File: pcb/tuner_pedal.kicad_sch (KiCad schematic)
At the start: 35 parts, among them J1 SWD, J2 Fermion 1.8" TFT LCD, J3 UART, J4 Potentiometer, SW1 SW_Push, SW2 SW_Push, U1 STM32F411CEUx, Y1 25MHz 9pF

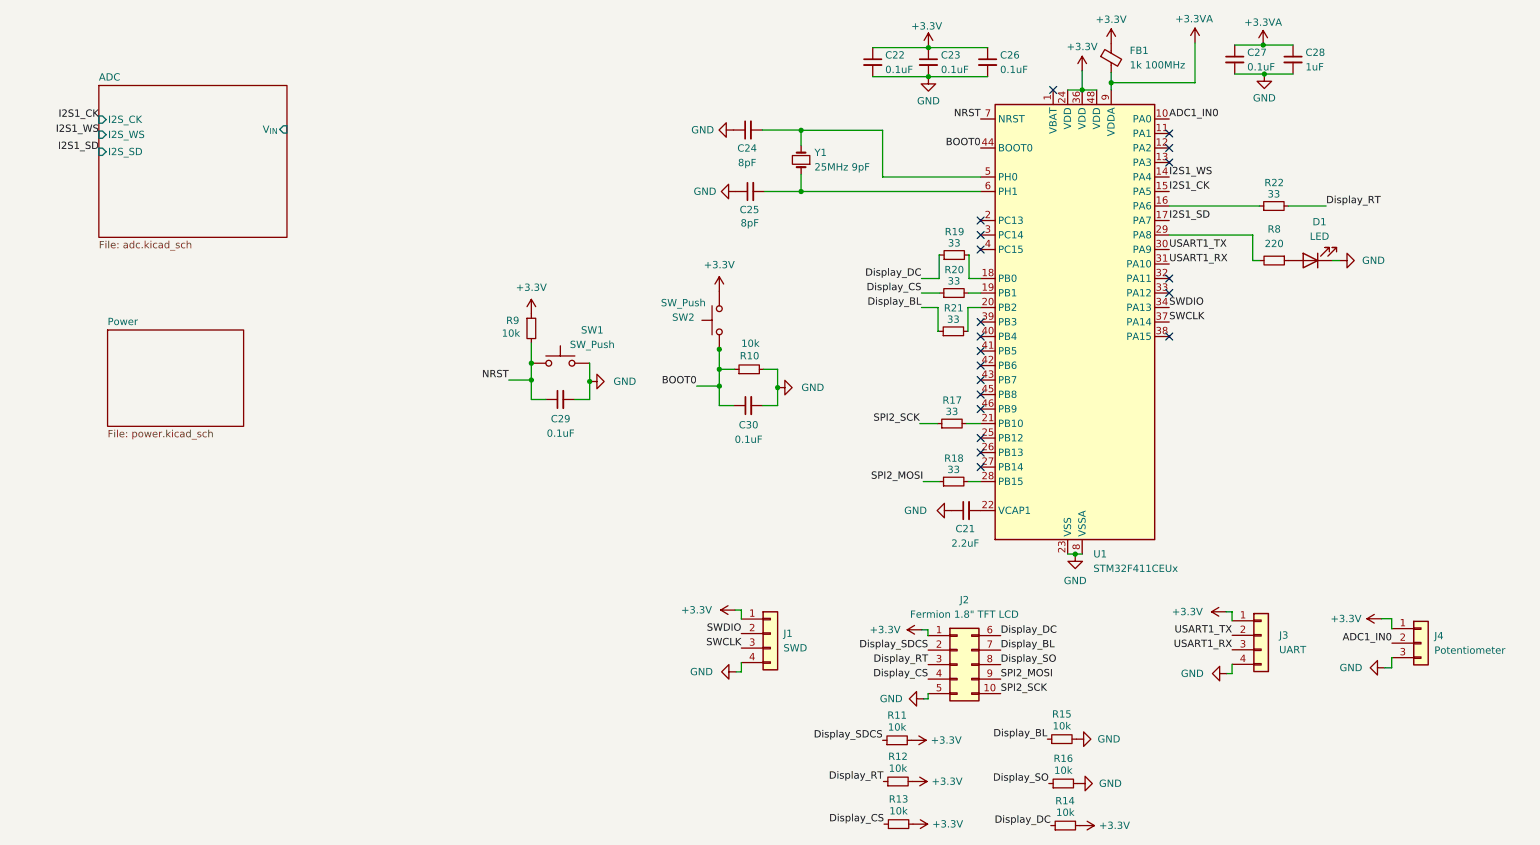
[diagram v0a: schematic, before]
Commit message: Made MCU sheet
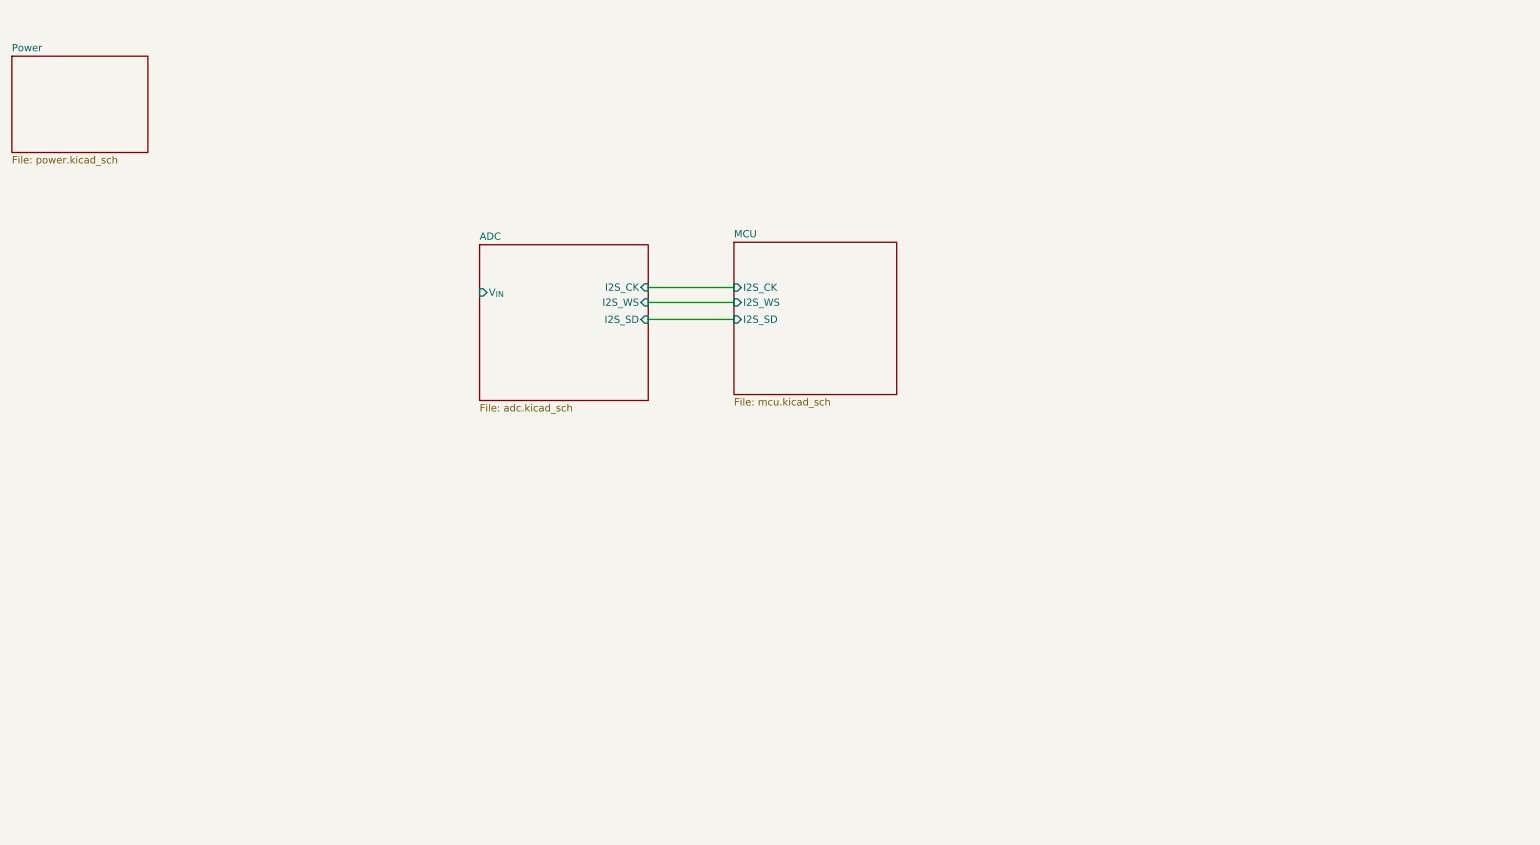
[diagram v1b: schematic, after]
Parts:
- removed C21: 2.2uF, symbol Device:C_Small
- removed C22, C23, C26, C27, C29, C30: 0.1uF, symbol Device:C_Small
- removed C24, C25: 8pF, symbol Device:C_Small
- removed C28: 1uF, symbol Device:C_Small
- removed D1: LED, symbol Device:LED
- removed FB1: 1k 100MHz, symbol Device:FerriteBead_Small
- removed J1: SWD, Connector_PinHeader_2.54mm:PinHeader_1x04_P2.54mm_Vertical, symbol Connector_Generic:Conn_01x04
- removed J2: Fermion 1.8" TFT LCD, Connector_PinHeader_2.54mm:PinHeader_2x05_P2.54mm_Vertical, symbol Connector_Generic:Conn_02x05_Top_Bottom
- removed J3: UART, Connector_PinHeader_2.54mm:PinHeader_1x04_P2.54mm_Vertical, symbol Connector_Generic:Conn_01x04
- removed J4: Potentiometer, Connector_PinSocket_2.54mm:PinSocket_1x03_P2.54mm_Vertical, symbol Connector_Generic:Conn_01x03
- removed R10, R11, R12, R13, R14, R15, R16, R9: 10k, symbol Device:R_Small
- removed R17, R18, R19, R20, R21, R22: 33, symbol Device:R_Small
- removed R8: 220, symbol Device:R_Small
- removed SW1, SW2: SW_Push, Button_Switch_SMD:SW_SPST_Omron_B3FS-100xP, symbol Switch:SW_Push
- removed U1: STM32F411CEUx, Package_DFN_QFN:QFN-48-1EP_7x7mm_P0.5mm_EP5.6x5.6mm, symbol MCU_ST_STM32F4:STM32F411CEUx
- removed Y1: 25MHz 9pF, symbol Device:Crystal_Small
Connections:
- no-connect marks 20 -> 0
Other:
- added sheet MCU (mcu.kicad_sch)

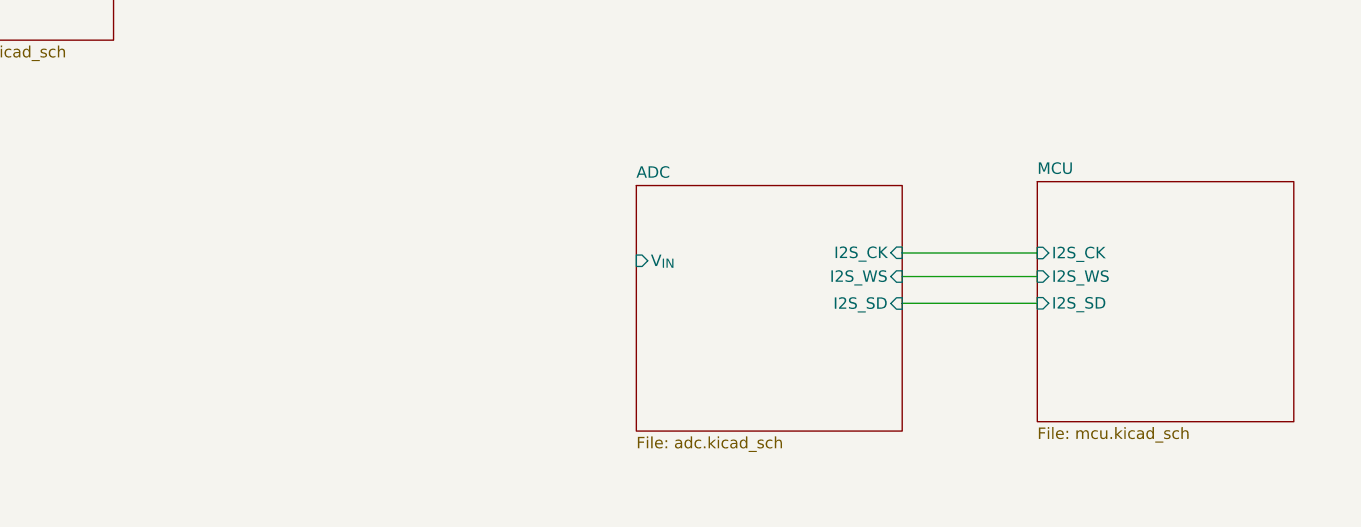
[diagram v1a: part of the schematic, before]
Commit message: Brought in analog frontend
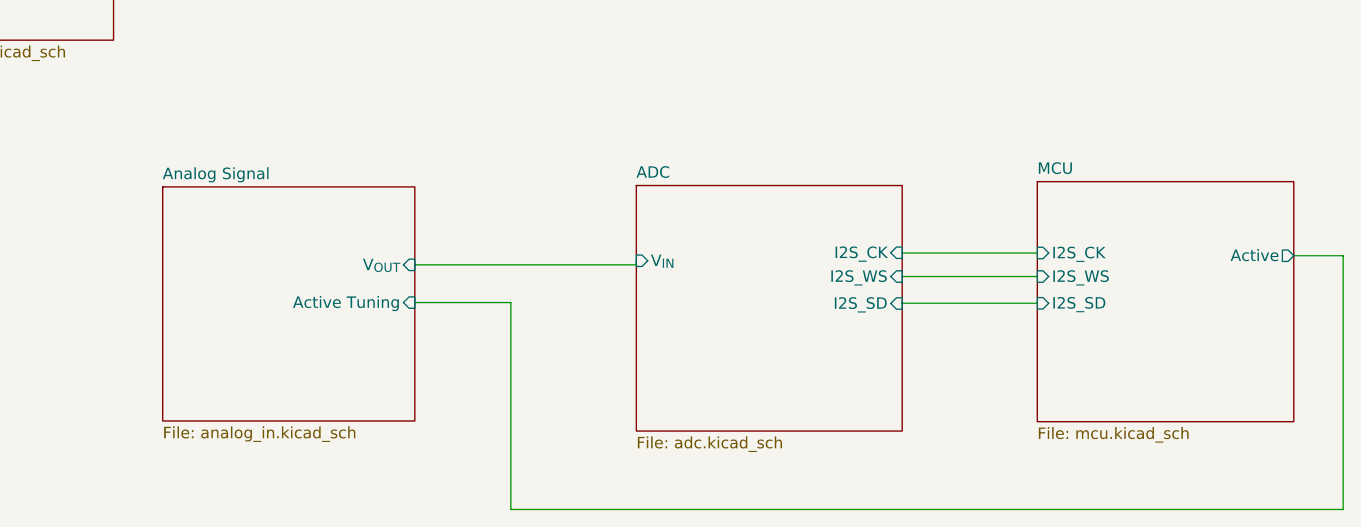
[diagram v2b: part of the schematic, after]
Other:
- added sheet Analog Signal (analog_in.kicad_sch)
- sheet MCU ports: added Active; removed none
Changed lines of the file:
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@@
+    (stroke (width 0) (type default))
+  )
+  (wire (pts (xy 103.3018 62.992) (xy 103.3018 62.5348))
+    (stroke (width 0) (type default))
+  )
+  (wire (pts (xy 89.3572 67.183) (xy 89.3572 90.17))
     (stroke (width 0) (type default))
   )
@@
     (stroke (width 0) (type default))
   )
+  (wire (pts (xy 181.8386 61.976) (xy 176.3522 61.976))
+    (stroke (width 0) (type default))
+  )
   (wire (pts (xy 132.842 61.6712) (xy 132.842 61.6458))
+    (stroke (width 0) (type default))
+  )
+  (wire (pts (xy 78.6892 67.183) (xy 89.3572 67.183))
     (stroke (width 0) (type default))
   )
@@
     (stroke (width 0) (type default))
   )
+  (wire (pts (xy 89.3572 90.17) (xy 181.8386 90.17))
+    (stroke (width 0) (type default))
+  )
   (wire (pts (xy 147.8534 61.6712) (xy 132.842 61.6712))
+    (stroke (width 0) (type default))
+  )
+  (wire (pts (xy 78.6892 62.992) (xy 103.3018 62.992))
+    (stroke (width 0) (type default))
+  )
+  (wire (pts (xy 181.8386 90.17) (xy 181.8386 61.976))
     (stroke (width 0) (type default))
   )
@@
       (effects (font (size 1.27 1.27)) (justify left))
     )
+    (pin "Active" output (at 176.3522 61.976 0)
+      (effects (font (size 1.27 1.27)) (justify right))
+    )
     (instances
       (project "tuner_pedal"
@@
       )
     )
+  )
+  (sheet (at 50.673 54.3306) (size 28.0162 26.0096) (fields_autoplaced)
+    (stroke (width 0.1524) (type solid))
+    (fill (color 0 0 0 0.0000))
+    (property "Sheetname" "Analog Signal" (at 50.673 53.619 0)
+      (effects (font (size 1.27 1.27)) (justify left bottom))
+    )
+    (property "Sheetfile" "analog_in.kicad_sch" (at 50.673 80.9248 0)
+      (effects (font (size 1.27 1.27)) (justify left top))
+    )
+    (pin "V_{OUT}" input (at 78.6892 62.992 0)
+      (effects (font (size 1.27 1.27)) (justify right))
+    )
+    (pin "Active Tuning" input (at 78.6892 67.183 0)
+      (effects (font (size 1.27 1.27)) (justify right))
+    )
+    (instances
+      (project "tuner_pedal"
+        (path "/be09f3cc-c79c-49de-93a4-4a01bf6bfbcf" (page "5"))
+      )
+    )
